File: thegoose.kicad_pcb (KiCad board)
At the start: 2 copper layers, 88.5 x 50.5 mm, 27 parts

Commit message: Start on PCB
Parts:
- removed BC1: ~, hexy:buck converter
- removed DRV_1, DRV_2, DRV_3: ~, hexy:drv8833
- added C10: 10uF, Capacitor_SMD:C_0805_2012Metric_Pad1.18x1.45mm_HandSolder, F.Cu at (83.6, 77.6)
- added C11: 100nF, Capacitor_SMD:C_0805_2012Metric_Pad1.18x1.45mm_HandSolder, F.Cu at (83.6, 80.9)
- added C12: 100uF, Capacitor_SMD:C_1206_3216Metric_Pad1.33x1.80mm_HandSolder, F.Cu at (91.5, 91.7)
- added C13: 2.2uF, Capacitor_SMD:C_0805_2012Metric_Pad1.18x1.45mm_HandSolder, F.Cu at (83.6, 84.3)
- added C14: 100nF, Capacitor_SMD:C_0805_2012Metric_Pad1.18x1.45mm_HandSolder, F.Cu at (136.3, 75.0)
- added C15: 10uF, Capacitor_SMD:C_0805_2012Metric_Pad1.18x1.45mm_HandSolder, F.Cu at (129.8, 79.7)
- added C16: 2.7nF, Capacitor_SMD:C_0805_2012Metric_Pad1.18x1.45mm_HandSolder, F.Cu at (145.5, 81.7)
- added C2: 2.2uF, Capacitor_SMD:C_0805_2012Metric_Pad1.18x1.45mm_HandSolder, F.Cu at (77.6, 74.2)
- added C3: 10uF, Capacitor_SMD:C_0805_2012Metric_Pad1.18x1.45mm_HandSolder, F.Cu at (77.6, 77.6)
- added C4: 100nF, Capacitor_SMD:C_0805_2012Metric_Pad1.18x1.45mm_HandSolder, F.Cu at (77.6, 80.9)
- added C5: 100uF, Capacitor_SMD:C_1206_3216Metric_Pad1.33x1.80mm_HandSolder, F.Cu at (98.2, 69.8)
- added C6: 10uF, Capacitor_SMD:C_0805_2012Metric_Pad1.18x1.45mm_HandSolder, F.Cu at (77.6, 84.3)
- added C7: 100nF, Capacitor_SMD:C_0805_2012Metric_Pad1.18x1.45mm_HandSolder, F.Cu at (83.6, 70.9)
- added C8: 100uF, Capacitor_SMD:C_1206_3216Metric_Pad1.33x1.80mm_HandSolder, F.Cu at (98.7, 80.8)
- added C9: 2.2uF, Capacitor_SMD:C_0805_2012Metric_Pad1.18x1.45mm_HandSolder, F.Cu at (83.6, 74.2)
- added L1: 3.6uH, Inductor_SMD:L_1210_3225Metric_Pad1.42x2.65mm_HandSolder, F.Cu at (141.3, 75.0)
- added R10: .33, Resistor_SMD:R_0805_2012Metric_Pad1.20x1.40mm_HandSolder, F.Cu at (75.0, 54.3)
- added R11: .33, Resistor_SMD:R_0805_2012Metric_Pad1.20x1.40mm_HandSolder, F.Cu at (75.0, 57.6)
- added R12: .33, Resistor_SMD:R_0805_2012Metric_Pad1.20x1.40mm_HandSolder, F.Cu at (75.0, 60.9)
- added R13: 10k, Resistor_SMD:R_0805_2012Metric_Pad1.20x1.40mm_HandSolder, F.Cu at (152.8, 73.2)
- added R14: 10k, Resistor_SMD:R_0805_2012Metric_Pad1.20x1.40mm_HandSolder, F.Cu at (150.5, 73.2)
- added R15: 10k, Resistor_SMD:R_0805_2012Metric_Pad1.20x1.40mm_HandSolder, F.Cu at (155.0, 73.2)
- added R16: 10k, Resistor_SMD:R_0805_2012Metric_Pad1.20x1.40mm_HandSolder, F.Cu at (157.2, 73.2)
- added R17: 10k, Resistor_SMD:R_0805_2012Metric_Pad1.20x1.40mm_HandSolder, F.Cu at (162.1, 72.0)
- added R18: 10k, Resistor_SMD:R_0805_2012Metric_Pad1.20x1.40mm_HandSolder, F.Cu at (165.4, 72.0)
- added R19: 10k, Resistor_SMD:R_0805_2012Metric_Pad1.20x1.40mm_HandSolder, F.Cu at (168.7, 72.0)
- added R20: 10k, Resistor_SMD:R_0805_2012Metric_Pad1.20x1.40mm_HandSolder, F.Cu at (172.1, 72.0)
- added R21: 10k, Resistor_SMD:R_0805_2012Metric_Pad1.20x1.40mm_HandSolder, F.Cu at (81.0, 67.5)
- added R22: 10k, Resistor_SMD:R_0805_2012Metric_Pad1.20x1.40mm_HandSolder, F.Cu at (86.9, 47.7)
- added R23: 10k, Resistor_SMD:R_0805_2012Metric_Pad1.20x1.40mm_HandSolder, F.Cu at (86.9, 51.0)
- added R24: 10k, Resistor_SMD:R_0805_2012Metric_Pad1.20x1.40mm_HandSolder, F.Cu at (86.9, 54.3)
- added R25: 200k, Resistor_SMD:R_0805_2012Metric_Pad1.20x1.40mm_HandSolder, F.Cu at (134.0, 84.8)
- added R26: 115k, Resistor_SMD:R_0805_2012Metric_Pad1.20x1.40mm_HandSolder, F.Cu at (142.2, 78.2)
- added R27: 22.1k, Resistor_SMD:R_0805_2012Metric_Pad1.20x1.40mm_HandSolder, F.Cu at (142.2, 85.0)
- added R28: 15.8k, Resistor_SMD:R_0805_2012Metric_Pad1.20x1.40mm_HandSolder, F.Cu at (142.2, 80.5)
- added R5: 10k, Resistor_SMD:R_0805_2012Metric_Pad1.20x1.40mm_HandSolder, F.Cu at (168.0, 63.2)
- added R6: 10k, Resistor_SMD:R_0805_2012Metric_Pad1.20x1.40mm_HandSolder, F.Cu at (178.2, 63.2)
- added R7: .33, Resistor_SMD:R_0805_2012Metric_Pad1.20x1.40mm_HandSolder, F.Cu at (69.1, 67.5)
- added R8: .33, Resistor_SMD:R_0805_2012Metric_Pad1.20x1.40mm_HandSolder, F.Cu at (75.0, 47.7)
- added R9: .33, Resistor_SMD:R_0805_2012Metric_Pad1.20x1.40mm_HandSolder, F.Cu at (75.0, 51.0)
- added U1: DRV8848, Package_SO:TSSOP-16-1EP_4.4x5mm_P0.65mm, F.Cu at (153.9, 80.0)
- added U2: DRV8848, Package_SO:TSSOP-16-1EP_4.4x5mm_P0.65mm, F.Cu at (163.0, 80.0)
- added U3: DRV8848, Package_SO:TSSOP-16-1EP_4.4x5mm_P0.65mm, F.Cu at (172.1, 80.0)
- added U4: AP64500SP-13, Package_SO:Diodes_SO-8EP, F.Cu at (136.5, 80.0)
- BT1: value Battery -> XT30_SOLDER_CABLE; footprint hexy:AMASS_XT60PW-M_1x02_P7.20mm_Horizontal -> hexy:XT30_SolderPads_1x02_P5.00mm
- C1: footprint Capacitor_SMD:C_1206_3216Metric_Pad1.33x1.80mm_HandSolder -> Capacitor_SMD:C_0805_2012Metric_Pad1.18x1.45mm_HandSolder
- R1, R2, R3, R4: footprint Resistor_SMD:R_1206_3216Metric_Pad1.30x1.75mm_HandSolder -> Resistor_SMD:R_0805_2012Metric_Pad1.20x1.40mm_HandSolder
- S1: value Motor_Servo -> IO_PORT_1
- S2: value Motor_Servo -> IO_PORT_2
- S3: value Motor_Servo -> IO_PORT_3
- S4: value Motor_Servo -> IO_PORT_4
- S5: value Motor_Servo -> IO_PORT_5
- S6: value Motor_Servo -> IO_PORT_6
- moved C1 90.3 mm to (77.6, 70.9), turned to 0 degrees
- moved R1 34.1 mm to (127.2, 63.2), turned to 90 degrees
- moved R2 33.3 mm to (137.5, 63.2), turned to -90 degrees
- moved R3 29.4 mm to (147.8, 63.2), turned to -90 degrees
- moved R4 22.4 mm to (158.0, 63.2), turned to -90 degrees
- moved BT1 11.8 mm to (124.5, 80.8)
- moved REF** 10.2 mm to (203.5, 110.2)
- moved REF** 10.2 mm to (122.0, 110.2)
- moved M6 10.2 mm to (176.0, 107.6)
- moved M5 10.0 mm to (166.6, 107.6)
- moved M4 9.91 mm to (157.1, 107.6)
- moved M3 9.87 mm to (147.7, 107.6)
- moved M2 9.77 mm to (138.2, 107.6)
- moved M1 9.66 mm to (128.8, 107.6)
- moved S6 4.16 mm to (178.2, 59.6)
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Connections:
- ESP32 pad 4: Net-(DRV_1-IN2) -> Net-(ESP32-D12)
- ESP32 pad 5: Net-(DRV_1-IN3) -> Net-(ESP32-D14)
- R1 pad 1: GND -> Net-(ESP32-D16)
- R1 pad 2: Net-(ESP32-D16) -> GND
- R2 pad 1: Net-(DRV_1-IN2) -> Net-(ESP32-D17)
- R3 pad 1: Net-(DRV_1-IN3) -> Net-(ESP32-D5)
- R4 pad 1: GND -> Net-(ESP32-D18)
- R4 pad 2: Net-(ESP32-D4) -> GND
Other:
- board size 88.5 x 50.5 mm -> 88.5 x 60.8 mm
- board text removed: "${REFERENCE}"

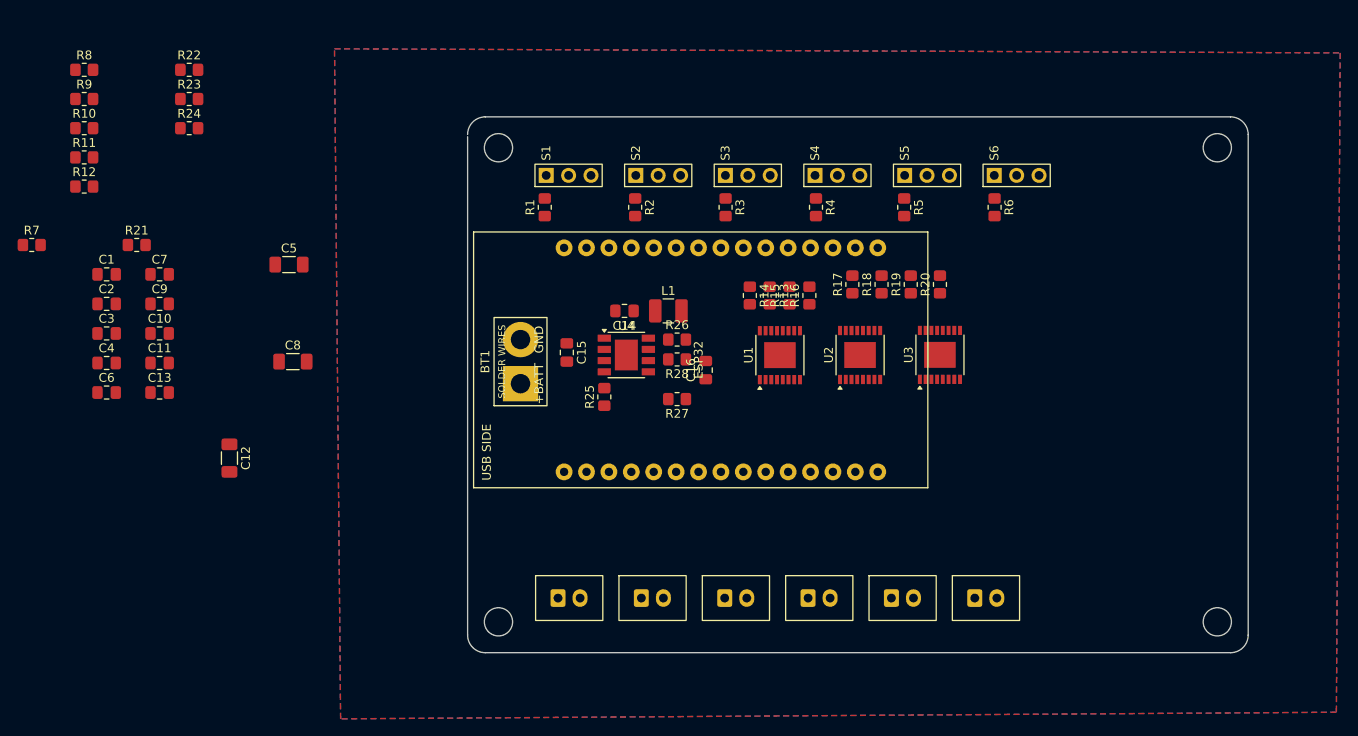
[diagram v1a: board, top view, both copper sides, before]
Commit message: Connect everything except GPIO
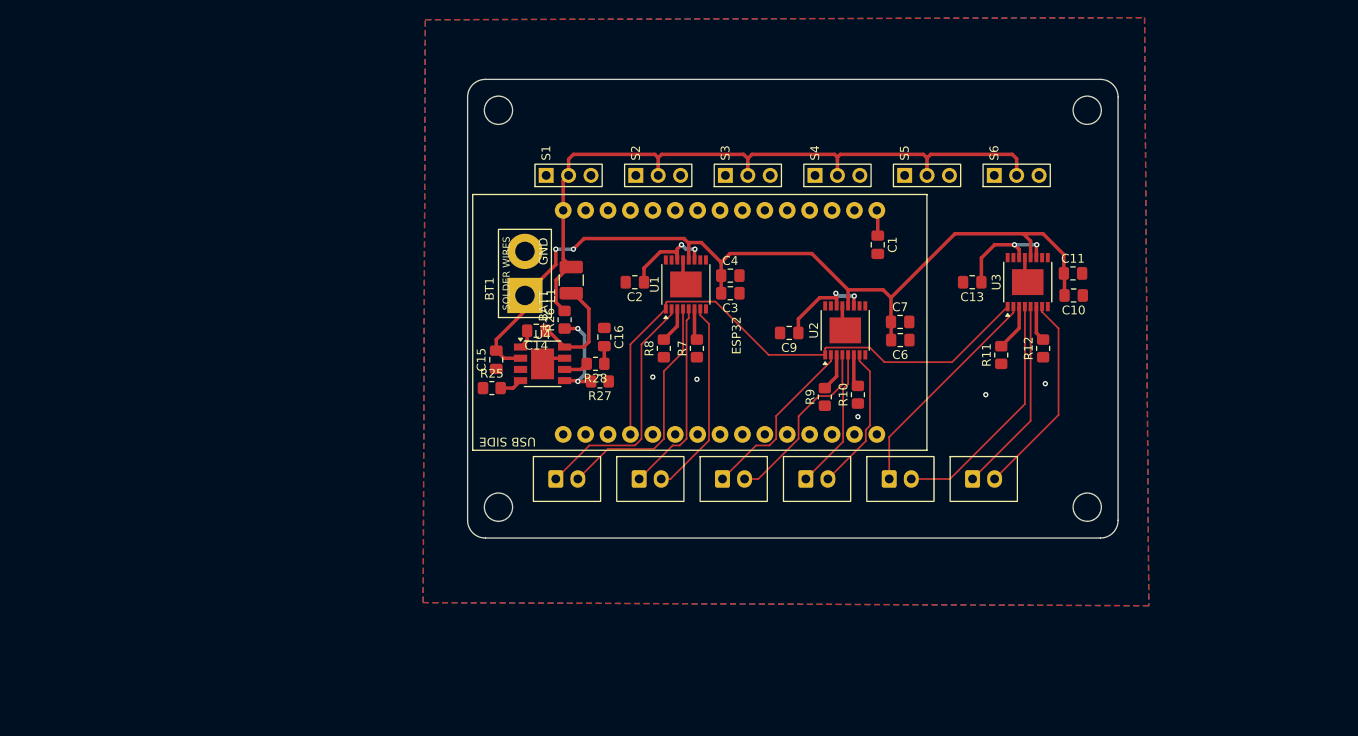
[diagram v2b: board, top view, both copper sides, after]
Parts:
- removed C12, C5, C8: 100uF, Capacitor_SMD:C_1206_3216Metric_Pad1.33x1.80mm_HandSolder
- removed R1, R13, R14, R15, R16, R17, R18, R19, R2, R20, R21, R22, R23, R24, R3, R4, R5, R6: 10k, Resistor_SMD:R_0805_2012Metric_Pad1.20x1.40mm_HandSolder
- removed the REF** at (203.5, 110.2)
- removed the REF** at (122.0, 56.5)
- removed the REF** at (122.0, 110.2)
- removed the REF** at (203.5, 56.5)
- added REF**: MountingHole_3.2mm_M3, MountingHole:MountingHole_3.2mm_M3, F.Cu at (122.0, 52.2)
- added REF**: MountingHole_3.2mm_M3, MountingHole:MountingHole_3.2mm_M3, F.Cu at (188.8, 52.2)
- added REF**: MountingHole_3.2mm_M3, MountingHole:MountingHole_3.2mm_M3, F.Cu at (188.8, 97.2)
- added REF**: MountingHole_3.2mm_M3, MountingHole:MountingHole_3.2mm_M3, F.Cu at (122.0, 97.2)
- moved R12 110.3 mm to (183.8, 79.2), turned to 90 degrees
- moved R11 106.4 mm to (179.0, 80.0), turned to 90 degrees
- moved C11 104.0 mm to (187.1, 70.8)
- moved C10 103.7 mm to (187.2, 73.2), turned to 180 degrees
- moved C13 93.0 mm to (175.7, 71.8), turned to 180 degrees
- moved R10 92.8 mm to (162.8, 84.5), turned to 90 degrees
- moved R9 90.5 mm to (159.0, 84.8), turned to 90 degrees
- moved C6 90.2 mm to (167.6, 78.3), turned to 180 degrees
- moved C1 87.5 mm to (165.0, 67.5), turned to -90 degrees
- moved C7 84.1 mm to (167.5, 76.2)
- moved R7 76.3 mm to (144.5, 79.2), turned to 90 degrees
- moved R8 72.9 mm to (140.8, 79.2), turned to 90 degrees
- moved C9 71.5 mm to (155.0, 77.5), turned to 180 degrees
- moved C4 71.4 mm to (148.3, 71.0)
- moved C3 70.9 mm to (148.3, 73.0), turned to 180 degrees
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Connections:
- ESP32 pad 10: Net-(ESP32-D32) -> /ESP_D32
- ESP32 pad 16: Net-(ESP32-D23) -> /ESP_D23
- ESP32 pad 17: Net-(ESP32-D22) -> /ESP_D22
- ESP32 pad 20: Net-(ESP32-D21) -> /ESP_D21
- ESP32 pad 21: Net-(ESP32-D19) -> /ESP_D19
- ESP32 pad 22: Net-(ESP32-D18) -> /ESP_D18
- ESP32 pad 23: Net-(ESP32-D5) -> /ESP_D5
- ESP32 pad 24: Net-(ESP32-D17) -> /ESP_D17
- ESP32 pad 25: Net-(ESP32-D16) -> /ESP_D16
- ESP32 pad 26: Net-(ESP32-D4) -> /ESP_D4
- ESP32 pad 27: unconnected-(ESP32-D2-Pad27) -> /ESP_D2
- ESP32 pad 28: Net-(ESP32-D15) -> /ESP_D15
- ESP32 pad 3: Net-(ESP32-D13) -> /ESP_D13
- ESP32 pad 4: Net-(ESP32-D12) -> /ESP_D12
- ESP32 pad 5: Net-(ESP32-D14) -> /ESP_D14
- ESP32 pad 6: Net-(ESP32-D27) -> /ESP_D27
- ESP32 pad 7: Net-(ESP32-D26) -> /ESP_D26
- ESP32 pad 8: Net-(ESP32-D25) -> /ESP_D25
- ESP32 pad 9: Net-(ESP32-D33) -> /ESP_D33
- S1 pad 1: Net-(ESP32-D16) -> unconnected-(S1-Pin_1-Pad1)
- S2 pad 1: Net-(ESP32-D17) -> unconnected-(S2-Pin_1-Pad1)
- S3 pad 1: Net-(ESP32-D5) -> unconnected-(S3-Pin_1-Pad1)
- S4 pad 1: Net-(ESP32-D18) -> unconnected-(S4-Pin_1-Pad1)
- S5 pad 1: Net-(ESP32-D4) -> unconnected-(S5-Pin_1-Pad1)
- S6 pad 1: Net-(ESP32-D15) -> unconnected-(S6-Pin_1-Pad1)
- U1 pad 1: VCC -> /ESP_D2
- U1 pad 10: Net-(ESP32-D27) -> unconnected-(U1-BIN2-Pad10)
- U1 pad 15: Net-(ESP32-D12) -> unconnected-(U1-AIN2-Pad15)
- U1 pad 16: Net-(ESP32-D13) -> unconnected-(U1-AIN1-Pad16)
- U1 pad 5: Net-(M2-OUT2) -> Net-(M2-OUT1)
- U1 pad 7: Net-(M2-OUT1) -> Net-(M2-OUT2)
- U1 pad 9: Net-(ESP32-D14) -> unconnected-(U1-BIN1-Pad9)
- U2 pad 1: VCC -> /ESP_D2
- U2 pad 10: Net-(ESP32-D32) -> unconnected-(U2-BIN2-Pad10)
- U2 pad 15: Net-(ESP32-D25) -> unconnected-(U2-AIN2-Pad15)
- U2 pad 16: Net-(ESP32-D26) -> unconnected-(U2-AIN1-Pad16)
- U2 pad 5: Net-(M4-OUT2) -> Net-(M4-OUT1)
- U2 pad 7: Net-(M4-OUT1) -> Net-(M4-OUT2)
- U2 pad 9: Net-(ESP32-D33) -> unconnected-(U2-BIN1-Pad9)
- U3 pad 1: VCC -> /ESP_D2
- U3 pad 10: Net-(ESP32-D19) -> unconnected-(U3-BIN2-Pad10)
- U3 pad 15: Net-(ESP32-D22) -> unconnected-(U3-AIN2-Pad15)
- U3 pad 16: Net-(ESP32-D23) -> unconnected-(U3-AIN1-Pad16)
- U3 pad 5: Net-(M6-OUT2) -> Net-(M6-OUT1)
- U3 pad 7: Net-(M6-OUT1) -> Net-(M6-OUT2)
- U3 pad 9: Net-(ESP32-D21) -> unconnected-(U3-BIN1-Pad9)
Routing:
- net +BATT: track 0.00 -> 101.2 mm, vias 0 -> 2
- net VCC: track 0.00 -> 81.6 mm
- net /ESP_D2: track 0.00 -> 62.0 mm
- net Net-(M1-OUT1): track 0.00 -> 27.7 mm
- net Net-(M5-OUT2): track 0.00 -> 27.5 mm
- net Net-(M1-OUT2): track 0.00 -> 27.3 mm
- net Net-(M5-OUT1): track 0.00 -> 25.4 mm
- net Net-(M6-OUT2): track 0.00 -> 23.3 mm
- net Net-(M2-OUT2): track 0.00 -> 22.5 mm
- net Net-(M6-OUT1): track 0.00 -> 22.3 mm
- net Net-(M2-OUT1): track 0.00 -> 22.1 mm
- net Net-(M3-OUT2): track 0.00 -> 20.4 mm
- net Net-(M3-OUT1): track 0.00 -> 20.1 mm
- net Net-(M4-OUT2): track 0.00 -> 16.5 mm
- net Net-(M4-OUT1): track 0.00 -> 16.1 mm
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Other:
- board size 88.5 x 60.8 mm -> 73.8 x 52 mm

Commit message: First iteration of PCB
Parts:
- removed REF** (x4): MountingHole_3.2mm_M3, MountingHole:MountingHole_3.2mm_M3
- moved C10 16.0 mm to (171.2, 73.7), turned to -90 degrees
- moved C11 14.0 mm to (173.5, 73.7), turned to 90 degrees
- moved C7 12.1 mm to (155.8, 73.7), turned to 90 degrees
- moved R9 11.5 mm to (162.5, 73.8), turned to -90 degrees
- moved U3 11.3 mm to (176.3, 81.5), turned to -90 degrees
- moved R10 11.0 mm to (160.2, 73.8), turned to -90 degrees
- moved C6 10.6 mm to (158.0, 73.7), turned to -90 degrees
- moved R12 9.71 mm to (175.8, 73.8), turned to -90 degrees
- moved U1 9.25 mm to (144.0, 81.2), turned to -90 degrees
- moved C4 9.20 mm to (139.5, 73.7), turned to 90 degrees
- moved C13 8.20 mm to (167.8, 73.7), turned to 90 degrees
- moved R8 7.78 mm to (146.2, 73.8), turned to -90 degrees
- moved C3 6.58 mm to (141.8, 73.7), turned to -90 degrees
- moved R11 6.33 mm to (178.0, 73.8), turned to -90 degrees
- moved R7 5.52 mm to (144.0, 73.8), turned to -90 degrees
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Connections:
- S1 pad 1: unconnected-(S1-Pin_1-Pad1) -> /ESP_D13
- S2 pad 1: unconnected-(S2-Pin_1-Pad1) -> /ESP_D12
- S3 pad 1: unconnected-(S3-Pin_1-Pad1) -> /ESP_D26
- S4 pad 1: unconnected-(S4-Pin_1-Pad1) -> /ESP_D25
- S5 pad 1: unconnected-(S5-Pin_1-Pad1) -> /ESP_D33
- S6 pad 1: unconnected-(S6-Pin_1-Pad1) -> /ESP_D32
- U1 pad 10: unconnected-(U1-BIN2-Pad10) -> /ESP_D4
- U1 pad 15: unconnected-(U1-AIN2-Pad15) -> /ESP_D16
- U1 pad 16: unconnected-(U1-AIN1-Pad16) -> /ESP_D17
- U1 pad 2: Net-(M1-OUT1) -> Net-(M2-OUT1)
- U1 pad 4: Net-(M1-OUT2) -> Net-(M2-OUT2)
- U1 pad 5: Net-(M2-OUT1) -> Net-(M1-OUT1)
- U1 pad 7: Net-(M2-OUT2) -> Net-(M1-OUT2)
- U1 pad 9: unconnected-(U1-BIN1-Pad9) -> /ESP_D15
- U2 pad 10: unconnected-(U2-BIN2-Pad10) -> /ESP_D18
- U2 pad 15: unconnected-(U2-AIN2-Pad15) -> /ESP_D19
- U2 pad 16: unconnected-(U2-AIN1-Pad16) -> /ESP_D21
- U2 pad 2: Net-(M3-OUT1) -> Net-(M4-OUT1)
- U2 pad 4: Net-(M3-OUT2) -> Net-(M4-OUT2)
- U2 pad 5: Net-(M4-OUT1) -> Net-(M3-OUT1)
- U2 pad 7: Net-(M4-OUT2) -> Net-(M3-OUT2)
- U2 pad 9: unconnected-(U2-BIN1-Pad9) -> /ESP_D5
- U3 pad 10: unconnected-(U3-BIN2-Pad10) -> /ESP_D23
- U3 pad 15: unconnected-(U3-AIN2-Pad15) -> /ESP_D14
- U3 pad 16: unconnected-(U3-AIN1-Pad16) -> /ESP_D27
- U3 pad 2: Net-(M5-OUT1) -> Net-(M6-OUT1)
- U3 pad 4: Net-(M5-OUT2) -> Net-(M6-OUT2)
- U3 pad 5: Net-(M6-OUT1) -> Net-(M5-OUT1)
- U3 pad 7: Net-(M6-OUT2) -> Net-(M5-OUT2)
- U3 pad 9: unconnected-(U3-BIN1-Pad9) -> /ESP_D22
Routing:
- net /ESP_D14: track 0.00 -> 61.9 mm, vias 0 -> 2
- net /ESP_D27: track 0.00 -> 54.7 mm, vias 0 -> 1
- net +BATT: track 101.2 -> 130.2 mm, vias 2 -> 4
- net /ESP_D32: track 0.00 -> 27.7 mm, vias 0 -> 1
- net /ESP_D33: track 0.00 -> 21.7 mm
- net /ESP_D22: track 0.00 -> 13.7 mm, vias 0 -> 2
- net /ESP_D19: track 0.00 -> 12.8 mm, vias 0 -> 1
- net /ESP_D5: track 0.00 -> 12.7 mm, vias 0 -> 1
- net /ESP_D23: track 0.00 -> 12.5 mm, vias 0 -> 2
- net /ESP_D25: track 0.00 -> 12.4 mm
- net Net-(M4-OUT2): track 16.5 -> 28.8 mm, vias 0 -> 3
- net /ESP_D18: track 0.00 -> 11.5 mm, vias 0 -> 1
- net /ESP_D21: track 0.00 -> 11.3 mm, vias 0 -> 1
- net Net-(M4-OUT1): track 16.1 -> 27.2 mm, vias 0 -> 1
- net Net-(U3-VINT): track 12.8 -> 23.6 mm, vias 2 -> 4
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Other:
- board text added: "C4"

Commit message: Pass DRC
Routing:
- net /ESP_D13: track 9.40 -> 15.2 mm, vias 1 -> 0
- net /ESP_D14: vias 2 -> 3
- net GND: vias 0 -> 1
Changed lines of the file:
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@@
+		(net 3)
+	)
+	(via
+		(at 131.25 65.5)
+		(size 0.6)
+		(drill 0.3)
+		(layers "F.Cu" "B.Cu")
+		(free yes)
 		(net 3)
 	)
@@
 	(segment
 		(start 177 69.5)
-		(end 145.4 69.5)
+		(end 172 69.5)
 		(width 0.2)
 		(layer "F.Cu")
@@
 	)
 	(segment
+		(start 177.9675 84.29)
+		(end 177.9675 84.992)
+		(width 0.2)
+		(layer "F.Cu")
+		(net 48)
+	)
+	(segment
+		(start 177.9675 84.992)
+		(end 178.0915 85.116)
+		(width 0.2)
+		(layer "F.Cu")
+		(net 48)
+	)
+	(via
+		(at 182.5 83)
+		(size 0.6)
+		(drill 0.3)
+		(layers "F.Cu" "B.Cu")
+		(net 48)
+	)
+	(via
+		(at 172 69.5)
+		(size 0.6)
+		(drill 0.3)
+		(layers "F.Cu" "B.Cu")
+		(net 48)
+	)
+	(via
+		(at 177 69.5)
+		(size 0.6)
+		(drill 0.3)
+		(layers "F.Cu" "B.Cu")
+		(net 48)
+	)
+	(segment
+		(start 182.5 83)
+		(end 182.5 75)
+		(width 0.2)
+		(layer "B.Cu")
+		(net 48)
+	)
+	(segment
 		(start 145.4 69.5)
 		(end 139.5 63.6)
 		(width 0.2)
-		(layer "F.Cu")
+		(layer "B.Cu")
 		(net 48)
 	)
 	(segment
-		(start 177.9675 84.29)
-		(end 177.9675 84.992)
-		(width 0.2)
-		(layer "F.Cu")
-		(net 48)
-	)
-	(segment
-		(start 177.9675 84.992)
-		(end 178.0915 85.116)
-		(width 0.2)
-		(layer "F.Cu")
-		(net 48)
-	)
-	(via
-		(at 182.5 83)
-		(size 0.6)
-		(drill 0.3)
-		(layers "F.Cu" "B.Cu")
-		(net 48)
-	)
-	(via
-		(at 177 69.5)
-		(size 0.6)
-		(drill 0.3)
-		(layers "F.Cu" "B.Cu")
-		(net 48)
-	)
-	(segment
-		(start 182.5 83)
-		(end 182.5 75)
+		(start 172 69.5)
+		(end 145.4 69.5)
 		(width 0.2)
 		(layer "B.Cu")
@@
 	)
 	(segment
-		(start 127.41 59.635)
-		(end 127.41 60.91)
-		(width 0.2)
-		(layer "F.Cu")
+		(start 127.25 59.795)
+		(end 127.41 59.635)
+		(width 0.2)
+		(layer "B.Cu")
 		(net 52)
 	)
 	(segment
-		(start 127.41 60.91)
-		(end 128 61.5)
-		(width 0.2)
-		(layer "F.Cu")
+		(start 127.25 64.25)
+		(end 127.25 59.795)
+		(width 0.2)
+		(layer "B.Cu")
 		(net 52)
 	)
-	(via
-		(at 128 61.5)
-		(size 0.6)
-		(drill 0.3)
-		(layers "F.Cu" "B.Cu")
+	(segment
+		(start 134.42 63.6)
+		(end 134.42 65.33)
+		(width 0.2)
+		(layer "B.Cu")
 		(net 52)
 	)
 	(segment
-		(start 132.32 61.5)
-		(end 134.42 63.6)
+		(start 133 66.75)
+		(end 129.75 66.75)
 		(width 0.2)
 		(layer "B.Cu")
@@
 	)
 	(segment
-		(start 128 61.5)
-		(end 132.32 61.5)
-		(width 0.2)
-		(layer "B.Cu")
+		(start 129.75 66.75)
+		(end 127.25 64.25)
+		(width 0.2)
+		(layer "B.Cu")
+		(net 52)
+	)
+	(segment
+		(start 134.42 65.33)
+		(end 133 66.75)
+		(width 0.2)
+		(layer "B.Cu")
